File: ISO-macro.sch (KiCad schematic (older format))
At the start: 26 parts, among them J1 USB_C_Receptacle_USB2.0, SW1 SW_SPST, SW2 SW_SPST, SW3 SW_SPST, SW4 SW_SPST, SW5 SW_SPST, SW6 SW_SPST, SW7 SW_SPST, SW8 EC11, SW9 SW_SPST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

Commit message: add bom list
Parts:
- C1: LCSC (none) -> C301999
- C4, C5, C6: LCSC (none) -> C301997
- D1, D2, D3: footprint LED_SMD:LED_WS2812B_PLCC4_5.0x5.0mm_P3.2mm -> LED_SMD:LED_SK6812MINI_PLCC4_3.5x3.5mm_P1.75mm; LCSC (none) -> C527089
- F1: LCSC (none) -> C883119
- J1: LCSC (none) -> C167321
- R1, R4: LCSC (none) -> C140214
- R2, R3: LCSC (none) -> C258121
- R5, R6: LCSC (none) -> C294638
- U1: LCSC (none) -> C17317
- Y1: LCSC (none) -> C341521
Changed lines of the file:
@@
 F 2 "Connector_USB:USB_C_Receptacle_HRO_TYPE-C-31-M-12" H 1400 1750 50  0001 C CNN
 F 3 "https://www.usb.org/sites/default/files/documents/usb_type-c.zip" H 1400 1750 50  0001 C CNN
+F 4 "C167321" H 1250 1750 50  0001 C CNN "LCSC"
 	1    1250 1750
 	1    0    0    -1
@@
 F 2 "Resistor_SMD:R_0402_1005Metric" V 4530 5350 50  0001 C CNN
 F 3 "~" H 4600 5350 50  0001 C CNN
+F 4 "C140214" H 4600 5350 50  0001 C CNN "LCSC"
 	1    4600 5350
 	0    1    1    0
@@
 F 2 "Resistor_SMD:R_0402_1005Metric" V 2730 3750 50  0001 C CNN
 F 3 "~" H 2800 3750 50  0001 C CNN
+F 4 "C258121" H 2800 3750 50  0001 C CNN "LCSC"
 	1    2800 3750
 	0    1    1    0
@@
 F 2 "Resistor_SMD:R_0402_1005Metric" V 2730 3850 50  0001 C CNN
 F 3 "~" H 2800 3850 50  0001 C CNN
+F 4 "C258121" H 2800 3850 50  0001 C CNN "LCSC"
 	1    2800 3850
 	0    1    1    0
@@
 F 2 "Capacitor_SMD:C_0402_1005Metric" H 2788 4050 50  0001 C CNN
 F 3 "~" H 2750 4200 50  0001 C CNN
+F 4 "C301999" H 2750 4200 50  0001 C CNN "LCSC"
 	1    2750 4200
 	1    0    0    -1
@@
 F 2 "Crystal:Resonator_SMD_muRata_CSTxExxV-3Pin_3.0x1.1mm" H 975 3600 50  0001 C CNN
 F 3 "~" H 975 3600 50  0001 C CNN
+F 4 "C341521" H 1000 3600 50  0001 C CNN "LCSC"
 	1    1000 3600
 	1    0    0    -1
@@
 F 2 "Resistor_SMD:R_0402_1005Metric" V 1330 4250 50  0001 C CNN
 F 3 "~" H 1400 4250 50  0001 C CNN
+F 4 "C140214" H 1400 4250 50  0001 C CNN "LCSC"
 	1    1400 4250
 	0    1    1    0
@@
 F 2 "Resistor_SMD:R_0402_1005Metric" V 1930 1350 50  0001 C CNN
 F 3 "~" H 2000 1350 50  0001 C CNN
+F 4 "C294638" H 2000 1350 50  0001 C CNN "LCSC"
 	1    2000 1350
 	0    1    1    0
@@
 F 2 "Resistor_SMD:R_0402_1005Metric" V 1930 1450 50  0001 C CNN
 F 3 "~" H 2000 1450 50  0001 C CNN
+F 4 "C294638" H 2000 1450 50  0001 C CNN "LCSC"
 	1    2000 1450
 	0    1    1    0
@@
 F 2 "Fuse:Fuse_1206_3216Metric" H 2200 950 50  0001 L CNN
 F 3 "~" H 2150 1150 50  0001 C CNN
+F 4 "C883119" H 2150 1150 50  0001 C CNN "LCSC"
 	1    2150 1150
 	0    1    1    0
@@
 F 0 "D1" H 6794 3496 50  0000 L CNN
 F 1 "WS2812B" H 6794 3405 50  0000 L CNN
-F 2 "LED_SMD:LED_WS2812B_PLCC4_5.0x5.0mm_P3.2mm" H 6500 3150 50  0001 L TNN
+F 2 "LED_SMD:LED_SK6812MINI_PLCC4_3.5x3.5mm_P1.75mm" H 6500 3150 50  0001 L TNN
 F 3 "https://cdn-shop.adafruit.com/datasheets/WS2812B.pdf" H 6550 3075 50  0001 L TNN
+F 4 "C527089" H 6450 3450 50  0001 C CNN "LCSC"
 	1    6450 3450
 	1    0    0    -1
@@
 F 0 "D2" H 7694 3496 50  0000 L CNN
 F 1 "WS2812B" H 7694 3405 50  0000 L CNN
-F 2 "LED_SMD:LED_WS2812B_PLCC4_5.0x5.0mm_P3.2mm" H 7400 3150 50  0001 L TNN
+F 2 "LED_SMD:LED_SK6812MINI_PLCC4_3.5x3.5mm_P1.75mm" H 7400 3150 50  0001 L TNN
 F 3 "https://cdn-shop.adafruit.com/datasheets/WS2812B.pdf" H 7450 3075 50  0001 L TNN
+F 4 "C527089" H 7350 3450 50  0001 C CNN "LCSC"
 	1    7350 3450
 	1    0    0    -1
@@
 F 0 "D3" H 8594 3496 50  0000 L CNN
 F 1 "WS2812B" H 8594 3405 50  0000 L CNN
-F 2 "LED_SMD:LED_WS2812B_PLCC4_5.0x5.0mm_P3.2mm" H 8300 3150 50  0001 L TNN
+F 2 "LED_SMD:LED_SK6812MINI_PLCC4_3.5x3.5mm_P1.75mm" H 8300 3150 50  0001 L TNN
 F 3 "https://cdn-shop.adafruit.com/datasheets/WS2812B.pdf" H 8350 3075 50  0001 L TNN
+F 4 "C527089" H 8250 3450 50  0001 C CNN "LCSC"
 	1    8250 3450
 	1    0    0    -1
@@
 F 2 "Capacitor_SMD:C_0402_1005Metric" H 7738 3050 50  0001 C CNN
 F 3 "~" H 7700 3200 50  0001 C CNN
+F 4 "C301997" H 7700 3200 50  0001 C CNN "LCSC"
 	1    7700 3200
 	1    0    0    -1
@@
 F 2 "Capacitor_SMD:C_0402_1005Metric" H 8638 3050 50  0001 C CNN
 F 3 "~" H 8600 3200 50  0001 C CNN
+F 4 "C301997" H 8600 3200 50  0001 C CNN "LCSC"
 	1    8600 3200
 	1    0    0    -1
@@
 F 2 "Capacitor_SMD:C_0402_1005Metric" H 6838 3050 50  0001 C CNN
 F 3 "~" H 6800 3200 50  0001 C CNN
+F 4 "C301997" H 6800 3200 50  0001 C CNN "LCSC"
 	1    6800 3200
 	1    0    0    -1
@@
 F 2 "Package_DFN_QFN:QFN-32-1EP_5x5mm_P0.5mm_EP3.1x3.1mm" H 3750 4250 50  0001 C CIN
 F 3 "http://ww1.microchip.com/downloads/en/DeviceDoc/doc7799.pdf" H 3750 4250 50  0001 C CNN
+F 4 "C17317" H 3750 4250 50  0001 C CNN "LCSC"
 	1    3750 4250
 	1    0    0    -1

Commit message: Add power caps, LEDs, finish routing (#3)
* wip

* Add LEDs and power caps, routing

* rm unuseds

* Add NCs where appropriate
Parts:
- added C2, C3, C7, C9: 100nF, Capacitor_SMD:C_0402_1005Metric, symbol Device:C
- added C8: 10uF, Capacitor_SMD:C_0402_1005Metric, symbol Device:C
- added D4, D5, D6: WS2812B, LED_SMD:LED_SK6812MINI_PLCC4_3.5x3.5mm_P1.75mm, symbol LED:WS2812B
- J1: symbol Connector:USB_C_Receptacle_USB2.0 -> ISO-macro-rescue:USB_C_Receptacle_USB2.0-Connector-ISO-macro-rescue
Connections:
- net EncB: now also U1.6 (PD0); no longer U1.26 (PC4)
- net GND: now also C2.2, C3.2, C7.2, C8.2, C9.2, D4.3 (VSS), D5.3 (VSS), D6.3 (VSS)
- net VCC: now also C2.1, C3.1, C7.1, C8.1, C9.1, D4.1 (VDD), D5.1 (VDD), D6.1 (VDD)
- net encsw: now also U1.23 (PC6); no longer U1.20 (PB6)
- net at SW3.2 (B): now also U1.11 (PD5); no longer U1.6 (PD0)
- net at SW5.2 (B): now also U1.12 (PD6); no longer U1.7 (PD1)
- net at SW6.2 (B): now also U1.9 (PD3); no longer U1.15 (PB1)
- net at SW4.2 (B): now also U1.8 (PD2); no longer U1.16 (PB2)
- net at SW2.2 (B): now also U1.7 (PD1); no longer U1.19 (PB5)
- net at SW1.2 (B): now also U1.10 (PD4); no longer U1.23 (PC6)
- net at D3.2 (DOUT): now also D4.4 (DIN)
- new net: D4.2 (DOUT), D5.4 (DIN)
- new net: D5.2 (DOUT), D6.4 (DIN)
- no-connect marks 3 -> 13
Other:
- moved on the sheet: C4, C5, C6, D1, D2, D3, SW1, SW2, SW3, SW4, SW5, SW6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

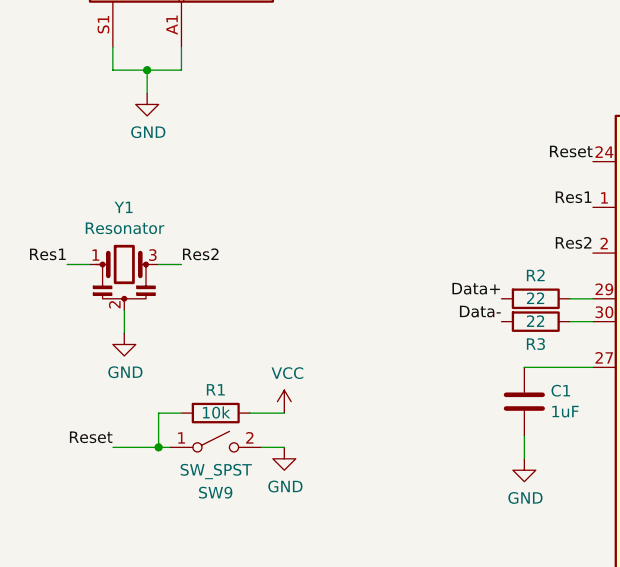
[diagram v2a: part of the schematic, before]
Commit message: update bom, change from integrated resonator to crystal
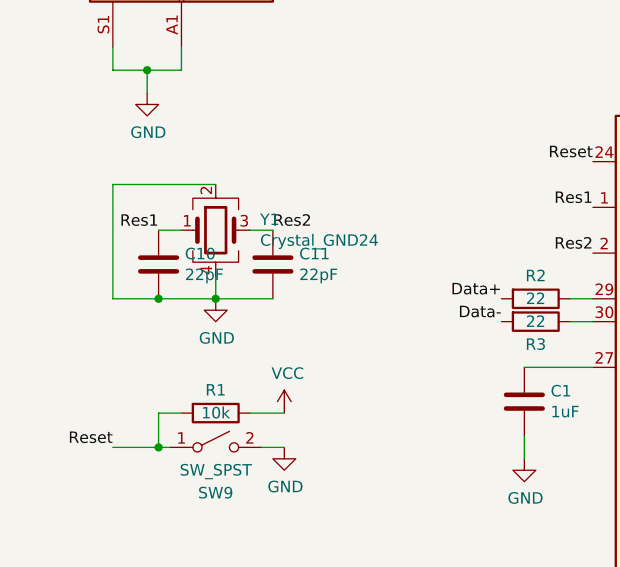
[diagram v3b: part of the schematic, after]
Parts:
- removed Y1: Resonator, Crystal:Resonator_SMD_muRata_CSTxExxV-3Pin_3.0x1.1mm, symbol Device:Resonator
- added C10, C11: 22pF, Capacitor_SMD:C_0402_1005Metric, symbol Device:C
- added Y1: Crystal_GND24, Crystal:Crystal_SMD_3225-4Pin_3.2x2.5mm, symbol Device:Crystal_GND24
- C8: LCSC (none) -> C15525
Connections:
- net GND: now also C10.2, C11.2, Y1.2, Y1.4
- net Res1: now also C10.1, Y1.1
- net Res2: now also C11.1, Y1.3
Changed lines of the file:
@@
 	2750 4450 2750 4350
-$Comp
-L Device:Resonator Y1
-U 1 1 60BA508B
-P 1000 3600
-F 0 "Y1" H 1000 3848 50  0000 C CNN
-F 1 "Resonator" H 1000 3757 50  0000 C CNN
-F 2 "Crystal:Resonator_SMD_muRata_CSTxExxV-3Pin_3.0x1.1mm" H 975 3600 50  0001 C CNN
-F 3 "~" H 975 3600 50  0001 C CNN
-F 4 "C341521" H 1000 3600 50  0001 C CNN "LCSC"
-	1    1000 3600
-	1    0    0    -1
-$EndComp
 $Comp
 L power:GND #PWR0107
 U 1 1 60BA817C
-P 1000 3900
-F 0 "#PWR0107" H 1000 3650 50  0001 C CNN
-F 1 "GND" H 1005 3727 50  0000 C CNN
-F 2 "" H 1000 3900 50  0001 C CNN
-F 3 "" H 1000 3900 50  0001 C CNN
-	1    1000 3900
-	1    0    0    -1
-$EndComp
-Wire Wire Line
-	1000 3900 1000 3800
+P 1400 3750
+F 0 "#PWR0107" H 1400 3500 50  0001 C CNN
+F 1 "GND" H 1405 3577 50  0000 C CNN
+F 2 "" H 1400 3750 50  0001 C CNN
+F 3 "" H 1400 3750 50  0001 C CNN
+	1    1400 3750
+	1    0    0    -1
+$EndComp
+Wire Wire Line
+	1400 3750 1400 3650
 Text Label 3050 3550 2    50   ~ 0
 Res2
 Text Label 3050 3350 2    50   ~ 0
 Res1
-Text Label 750  3600 2    50   ~ 0
+Text Label 1150 3450 2    50   ~ 0
 Res1
 Wire Wire Line
-	750  3600 850  3600
-Text Label 1250 3600 0    50   ~ 0
+	1150 3450 1250 3450
+Text Label 1650 3450 0    50   ~ 0
 Res2
 Wire Wire Line
-	1250 3600 1150 3600
+	1650 3450 1550 3450
 Text Label 3050 3150 2    50   ~ 0
 Reset
@@
 F 2 "Capacitor_SMD:C_0402_1005Metric" H 3238 1250 50  0001 C CNN
 F 3 "~" H 3200 1400 50  0001 C CNN
+F 4 "C15525" H 3200 1400 50  0001 C CNN "LCSC"
 	1    3200 1400
 	1    0    0    -1
@@
 NoConn ~ 4450 4250
 NoConn ~ 4450 4450
+$Comp
+L Device:Crystal_GND24 Y1
+U 1 1 60CA37A9
+P 1400 3450
+F 0 "Y1" H 1594 3496 50  0000 L CNN
+F 1 "Crystal_GND24" H 1594 3405 50  0000 L CNN
+F 2 "Crystal:Crystal_SMD_3225-4Pin_3.2x2.5mm" H 1400 3450 50  0001 C CNN
+F 3 "~" H 1400 3450 50  0001 C CNN
+F 4 "C13738" H 1400 3450 50  0001 C CNN "LCSC"
+	1    1400 3450
+	1    0    0    -1
+$EndComp
+$Comp
+L Device:C C11
+U 1 1 60CA5748
+P 1650 3600
+F 0 "C11" H 1765 3646 50  0000 L CNN
+F 1 "22pF" H 1765 3555 50  0000 L CNN
+F 2 "Capacitor_SMD:C_0402_1005Metric" H 1688 3450 50  0001 C CNN
+F 3 "~" H 1650 3600 50  0001 C CNN
+F 4 "C183675" H 1650 3600 50  0001 C CNN "LCSC"
+	1    1650 3600
+	1    0    0    -1
+$EndComp
+$Comp
+L Device:C C10
+U 1 1 60CA5D94
+P 1150 3600
+F 0 "C10" H 1265 3646 50  0000 L CNN
+F 1 "22pF" H 1265 3555 50  0000 L CNN
+F 2 "Capacitor_SMD:C_0402_1005Metric" H 1188 3450 50  0001 C CNN
+F 3 "~" H 1150 3600 50  0001 C CNN
+F 4 "C183675" H 1150 3600 50  0001 C CNN "LCSC"
+	1    1150 3600
+	1    0    0    -1
+$EndComp
+Wire Wire Line
+	1650 3750 1400 3750
+Connection ~ 1400 3750
+Wire Wire Line
+	1400 3750 1150 3750
+Wire Wire Line
+	1400 3250 950  3250
+Wire Wire Line
+	950  3250 950  3750
+Wire Wire Line
+	950  3750 1150 3750
+Connection ~ 1150 3750
 $EndSCHEMATC

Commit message: add missing part number
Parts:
- C9: LCSC (none) -> C301997
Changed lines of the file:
@@
 F 2 "Capacitor_SMD:C_0402_1005Metric" H 3838 1250 50  0001 C CNN
 F 3 "~" H 3800 1400 50  0001 C CNN
+F 4 "C301997" H 3800 1400 50  0001 C CNN "LCSC"
 	1    3800 1400
 	1    0    0    -1

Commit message: Change to basic, in-stock part numbers
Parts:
- C1: LCSC C301999 -> C52923
- C2, C3, C4, C5, C6, C7, C9: LCSC C301997 -> C1525
- F1: LCSC C883119 -> C70068
- R1, R4: LCSC C140214 -> C25744
- R2, R3: LCSC C258121 -> C25092
- R5, R6: LCSC C294638 -> C25905
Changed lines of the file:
@@
 F 2 "Resistor_SMD:R_0402_1005Metric" V 4530 5350 50  0001 C CNN
 F 3 "~" H 4600 5350 50  0001 C CNN
-F 4 "C140214" H 4600 5350 50  0001 C CNN "LCSC"
+F 4 "C25744" H 4600 5350 50  0001 C CNN "LCSC"
 	1    4600 5350
 	0    1    1    0
@@
 F 2 "Resistor_SMD:R_0402_1005Metric" V 2730 3750 50  0001 C CNN
 F 3 "~" H 2800 3750 50  0001 C CNN
-F 4 "C258121" H 2800 3750 50  0001 C CNN "LCSC"
+F 4 "C25092" H 2800 3750 50  0001 C CNN "LCSC"
 	1    2800 3750
 	0    1    1    0
@@
 F 2 "Resistor_SMD:R_0402_1005Metric" V 2730 3850 50  0001 C CNN
 F 3 "~" H 2800 3850 50  0001 C CNN
-F 4 "C258121" H 2800 3850 50  0001 C CNN "LCSC"
+F 4 "C25092" H 2800 3850 50  0001 C CNN "LCSC"
 	1    2800 3850
 	0    1    1    0
@@
 F 2 "Capacitor_SMD:C_0402_1005Metric" H 2788 4050 50  0001 C CNN
 F 3 "~" H 2750 4200 50  0001 C CNN
-F 4 "C301999" H 2750 4200 50  0001 C CNN "LCSC"
+F 4 "C52923" H 2750 4200 50  0001 C CNN "LCSC"
 	1    2750 4200
 	1    0    0    -1
@@
 F 2 "Resistor_SMD:R_0402_1005Metric" V 1330 4250 50  0001 C CNN
 F 3 "~" H 1400 4250 50  0001 C CNN
-F 4 "C140214" H 1400 4250 50  0001 C CNN "LCSC"
+F 4 "C25744" H 1400 4250 50  0001 C CNN "LCSC"
 	1    1400 4250
 	0    1    1    0
@@
 F 2 "Resistor_SMD:R_0402_1005Metric" V 1930 1350 50  0001 C CNN
 F 3 "~" H 2000 1350 50  0001 C CNN
-F 4 "C294638" H 2000 1350 50  0001 C CNN "LCSC"
+F 4 "C25905" H 2000 1350 50  0001 C CNN "LCSC"
 	1    2000 1350
 	0    1    1    0
@@
 F 2 "Resistor_SMD:R_0402_1005Metric" V 1930 1450 50  0001 C CNN
 F 3 "~" H 2000 1450 50  0001 C CNN
-F 4 "C294638" H 2000 1450 50  0001 C CNN "LCSC"
+F 4 "C25905" H 2000 1450 50  0001 C CNN "LCSC"
 	1    2000 1450
 	0    1    1    0
@@
 F 2 "Fuse:Fuse_1206_3216Metric" H 2200 950 50  0001 L CNN
 F 3 "~" H 2150 1150 50  0001 C CNN
-F 4 "C883119" H 2150 1150 50  0001 C CNN "LCSC"
+F 4 "C70068" H 2150 1150 50  0001 C CNN "LCSC"
 	1    2150 1150
 	0    1    1    0
@@
 F 2 "Capacitor_SMD:C_0402_1005Metric" H 7238 3050 50  0001 C CNN
 F 3 "~" H 7200 3200 50  0001 C CNN
-F 4 "C301997" H 7200 3200 50  0001 C CNN "LCSC"
+F 4 "C1525" H 7200 3200 50  0001 C CNN "LCSC"
 	1    7200 3200
 	1    0    0    -1
@@
 F 2 "Capacitor_SMD:C_0402_1005Metric" H 8138 3050 50  0001 C CNN
 F 3 "~" H 8100 3200 50  0001 C CNN
-F 4 "C301997" H 8100 3200 50  0001 C CNN "LCSC"
+F 4 "C1525" H 8100 3200 50  0001 C CNN "LCSC"
 	1    8100 3200
 	1    0    0    -1
@@
 F 2 "Capacitor_SMD:C_0402_1005Metric" H 6338 3050 50  0001 C CNN
 F 3 "~" H 6300 3200 50  0001 C CNN
-F 4 "C301997" H 6300 3200 50  0001 C CNN "LCSC"
+F 4 "C1525" H 6300 3200 50  0001 C CNN "LCSC"
 	1    6300 3200
 	1    0    0    -1
@@
 F 2 "Capacitor_SMD:C_0402_1005Metric" H 9038 3050 50  0001 C CNN
 F 3 "~" H 9000 3200 50  0001 C CNN
-F 4 "C301997" H 9000 3200 50  0001 C CNN "LCSC"
+F 4 "C1525" H 9000 3200 50  0001 C CNN "LCSC"
 	1    9000 3200
 	1    0    0    -1
@@
 F 2 "Capacitor_SMD:C_0402_1005Metric" H 9938 3050 50  0001 C CNN
 F 3 "~" H 9900 3200 50  0001 C CNN
-F 4 "C301997" H 9900 3200 50  0001 C CNN "LCSC"
+F 4 "C1525" H 9900 3200 50  0001 C CNN "LCSC"
 	1    9900 3200
 	1    0    0    -1
@@
 F 2 "Capacitor_SMD:C_0402_1005Metric" H 10838 3050 50  0001 C CNN
 F 3 "~" H 10800 3200 50  0001 C CNN
-F 4 "C301997" H 10800 3200 50  0001 C CNN "LCSC"
+F 4 "C1525" H 10800 3200 50  0001 C CNN "LCSC"
 	1    10800 3200
 	1    0    0    -1
@@
 F 2 "Capacitor_SMD:C_0402_1005Metric" H 3838 1250 50  0001 C CNN
 F 3 "~" H 3800 1400 50  0001 C CNN
-F 4 "C301997" H 3800 1400 50  0001 C CNN "LCSC"
+F 4 "C1525" H 3800 1400 50  0001 C CNN "LCSC"
 	1    3800 1400
 	1    0    0    -1

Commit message: smaller reset footprint, move a few things
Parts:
- SW9: footprint Button_Switch_THT:SW_PUSH_6mm -> TestPoint:TestPoint_2Pads_Pitch2.54mm_Drill0.8mm
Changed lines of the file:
@@
 F 0 "SW9" H 1400 4200 50  0000 C CNN
 F 1 "SW_SPST" H 1400 4300 50  0000 C CNN
-F 2 "Button_Switch_THT:SW_PUSH_6mm" H 1400 4400 50  0001 C CNN
+F 2 "TestPoint:TestPoint_2Pads_Pitch2.54mm_Drill0.8mm" H 1400 4400 50  0001 C CNN
 F 3 "~" H 1400 4400 50  0001 C CNN
 	1    1400 4400
